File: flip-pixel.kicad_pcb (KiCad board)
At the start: 2 copper layers, 225 parts, among them Q1 DMN62D0U-7, Q10 STS8DN6LF6AG, Q11 DMN62D0U-7, Q12 DMN62D0U-7, Q13 STS8DN6LF6AG, Q14 DMN62D0U-7, Q15 DMN62D0U-7, Q16 STS8DN6LF6AG, Q17 DMN62D0U-7, Q18 DMN62D0U-7, Q19 STS8DN6LF6AG, Q2 DMN62D0U-7, Q20 DMN62D0U-7, Q21 DMN62D0U-7, Q22 STS8DN6LF6AG, Q23 DMN62D0U-7, Q24 DMN62D0U-7, Q25 STS8DN6LF6AG, Q26 DMN62D0U-7, Q27 DMN62D0U-7, Q28 STS8DN6LF6AG, Q29 DMN62D0U-7, Q3 DMN62D0U-7, Q30 DMN62D0U-7, Q31 STS8DN6LF6AG, Q4 STS8DN6LF6AG, Q5 DMN62D0U-7, Q6 DMN62D0U-7, Q7 STS8DN6LF6AG, Q8 DMN62D0U-7, Q9 DMN62D0U-7, U1 LM2665M6

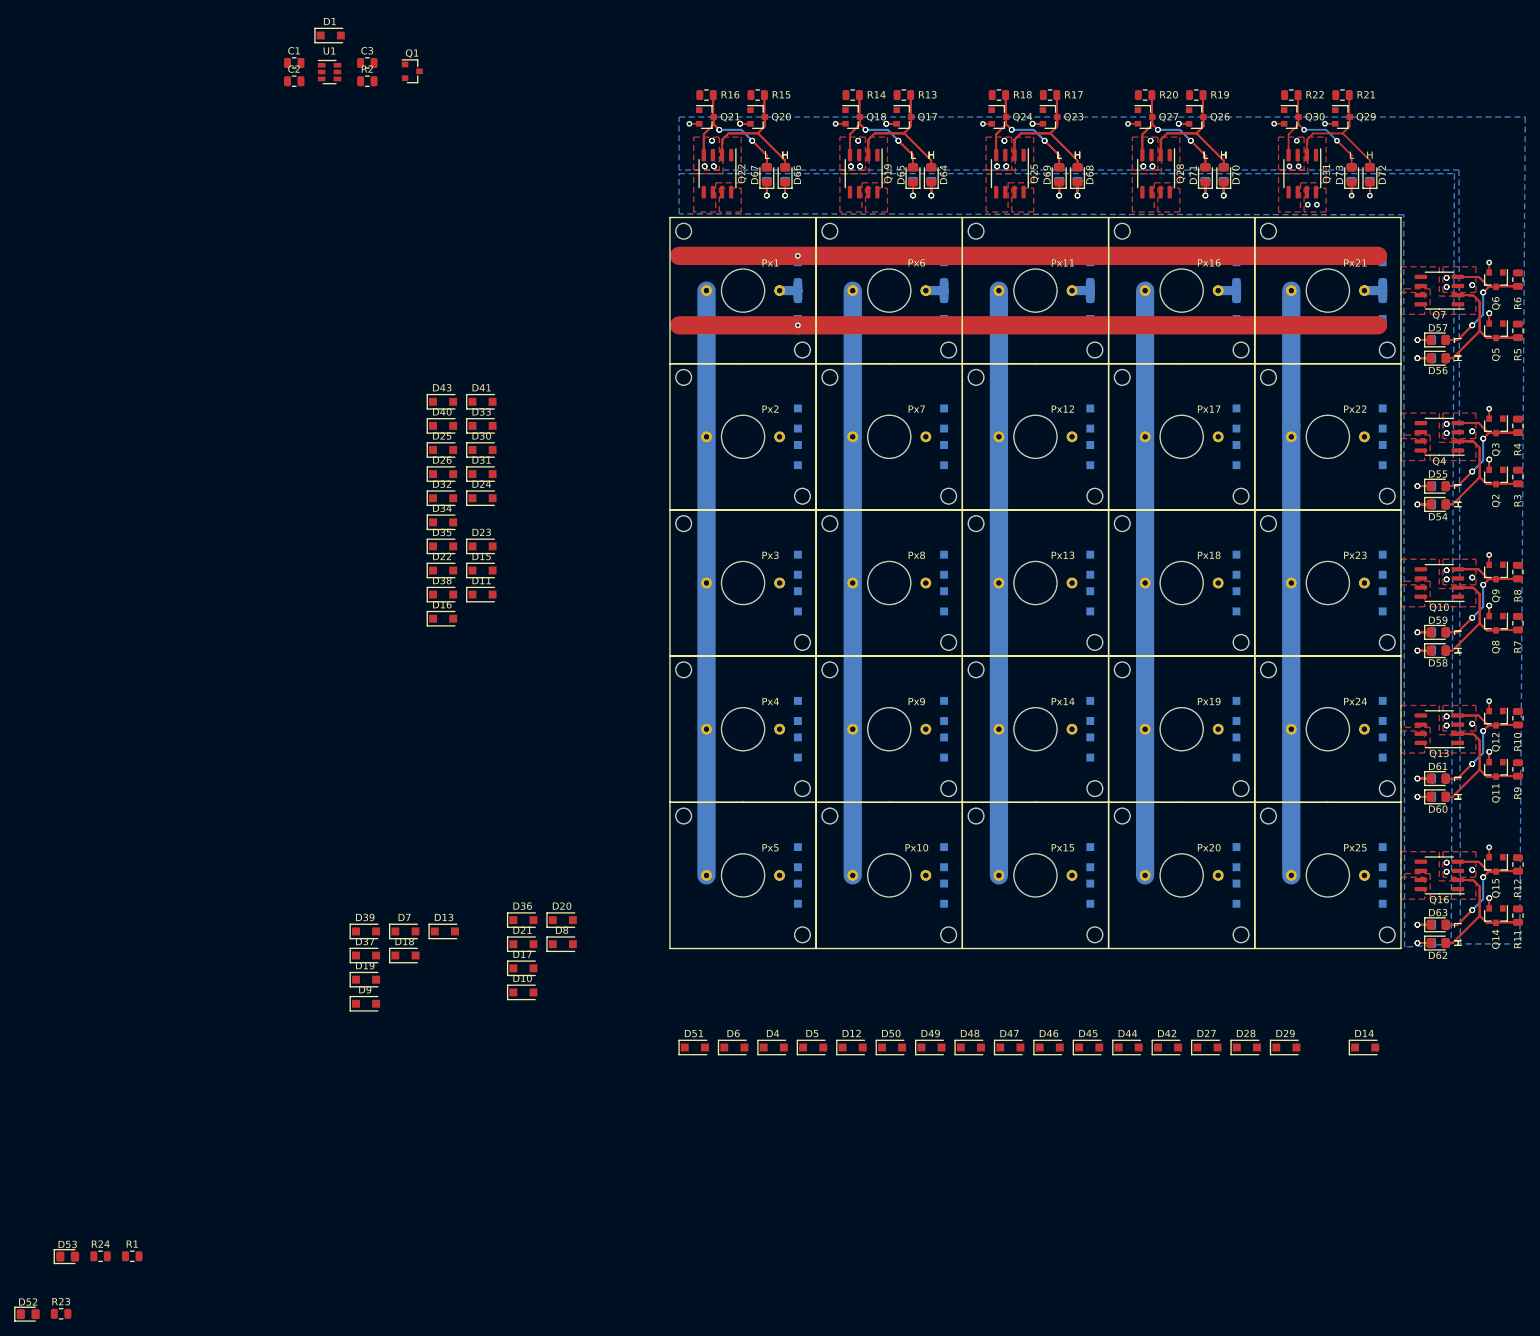
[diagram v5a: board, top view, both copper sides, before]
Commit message: adjustments for row drivers
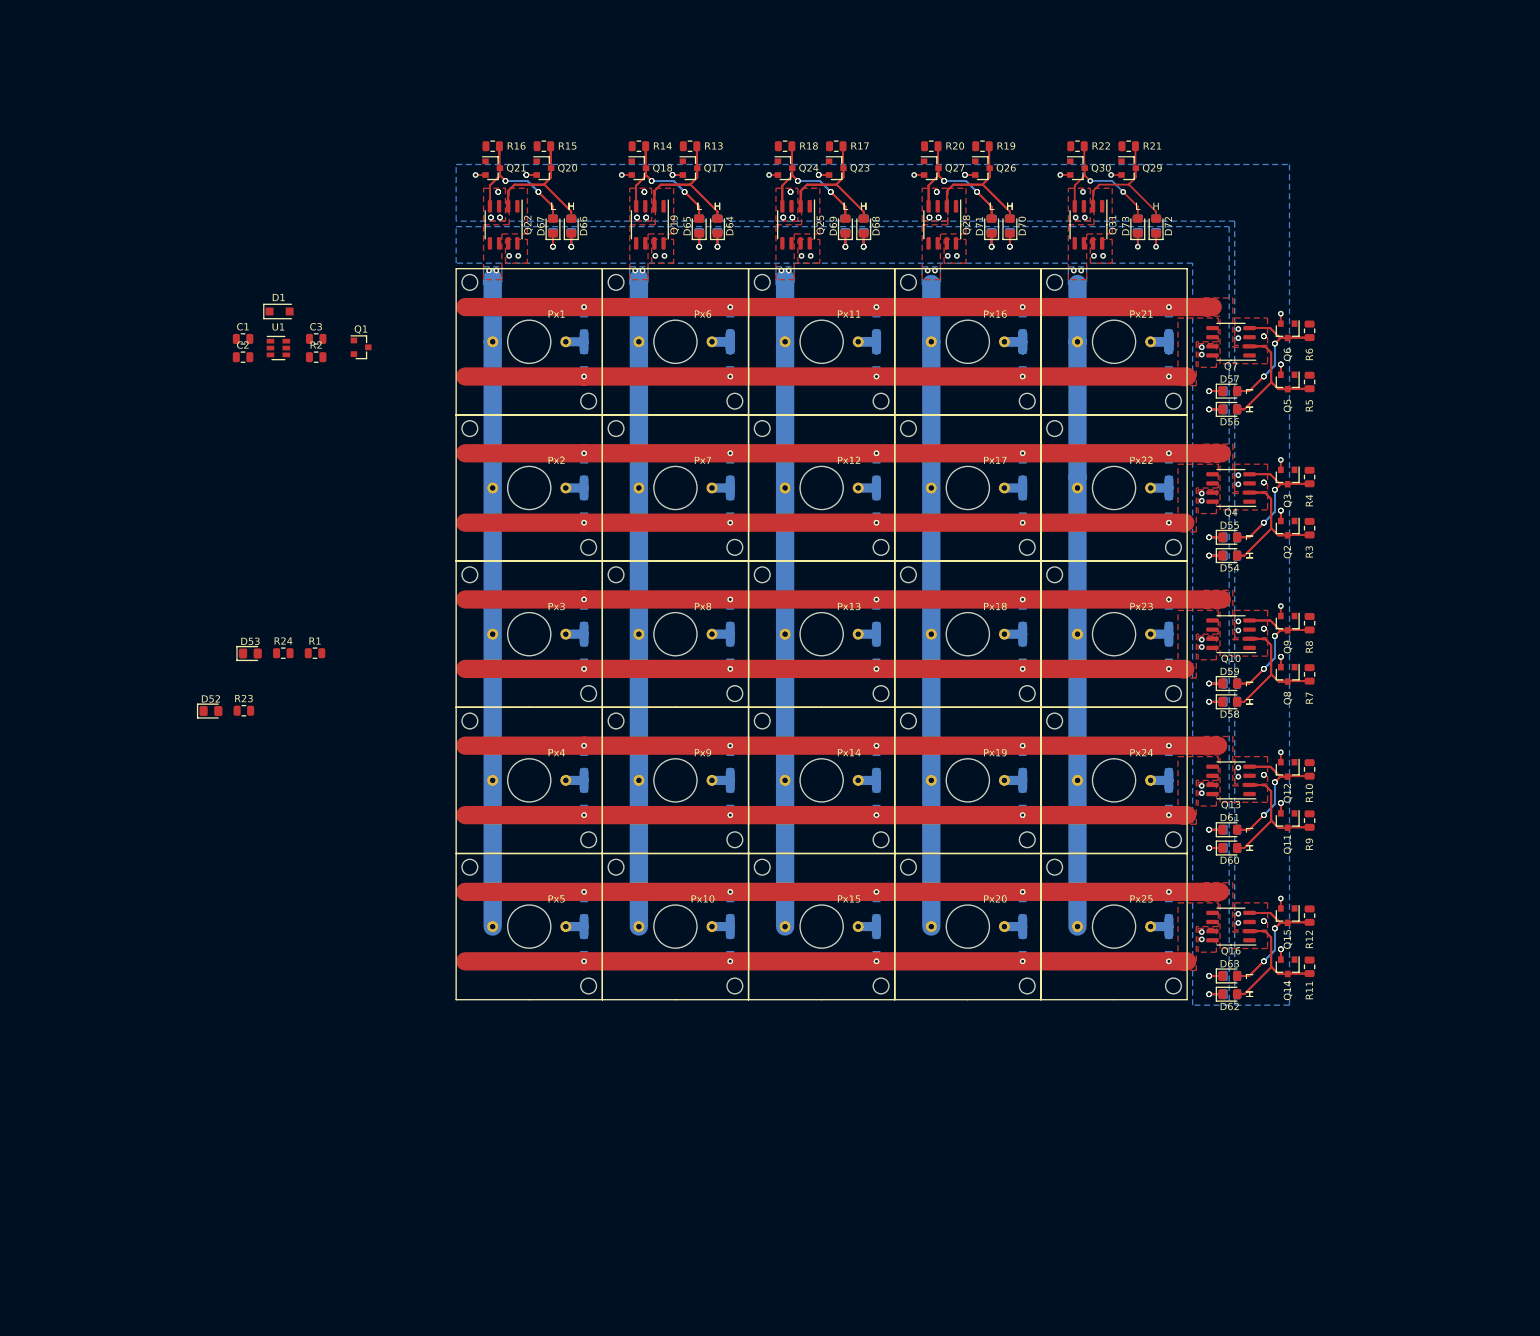
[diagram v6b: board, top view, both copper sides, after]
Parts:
- removed the D10 at (137.1, 149.6)
- removed the D11 at (131.4, 94.3)
- removed the D12 at (182.9, 157.3)
- removed the D13 at (126.2, 141.1)
- removed the D14 at (254.1, 157.3)
- removed the D15 at (131.4, 91.0)
- removed the D16 at (125.9, 97.7)
- removed the D17 at (137.1, 146.3)
- removed the D18 at (120.7, 144.5)
- removed the D19 at (115.2, 147.8)
- removed the D20 at (142.6, 139.6)
- removed the D21 at (137.1, 142.9)
- removed the D22 at (125.9, 91.0)
- removed the D23 at (131.4, 87.6)
- removed the D24 at (131.4, 80.9)
- removed the D25 at (125.9, 74.2)
- removed the D26 at (125.9, 77.6)
- removed the D27 at (232.2, 157.3)
- removed the D28 at (237.7, 157.3)
- removed the D29 at (243.1, 157.3)
- removed the D30 at (131.4, 74.2)
- removed the D31 at (131.4, 77.6)
- removed the D32 at (125.9, 80.9)
- removed the D33 at (131.4, 70.9)
- removed the D34 at (125.9, 84.3)
- removed the D35 at (125.9, 87.6)
- removed the D36 at (137.1, 139.6)
- removed the D37 at (115.2, 144.5)
- removed the D38 at (125.9, 94.3)
- removed the D39 at (115.2, 141.1)
- removed the D4 at (171.9, 157.3)
- removed the D40 at (125.9, 70.9)
- removed the D41 at (131.4, 67.5)
- removed the D42 at (226.7, 157.3)
- removed the D43 at (125.9, 67.5)
- removed the D44 at (221.2, 157.3)
- removed the D45 at (215.7, 157.3)
- removed the D46 at (210.3, 157.3)
- removed the D47 at (204.8, 157.3)
- removed the D48 at (199.3, 157.3)
- removed the D49 at (193.8, 157.3)
- removed the D5 at (177.4, 157.3)
- removed the D50 at (188.3, 157.3)
- removed the D51 at (160.9, 157.3)
- removed the D6 at (166.4, 157.3)
- removed the D7 at (120.7, 141.1)
- removed the D8 at (142.6, 142.9)
- removed the D9 at (115.2, 151.2)
- moved R1 87.6 mm to (108.1, 102.5)
- moved R23 87.6 mm to (98.3, 110.5)
- moved R24 87.6 mm to (103.7, 102.5)
- moved D52 87.6 mm to (93.7, 110.5)
- moved D53 87.6 mm to (99.2, 102.5)
- moved C1 39.0 mm to (98.1, 58.8)
- moved C2 39.0 mm to (98.1, 61.3)
- moved C3 39.0 mm to (108.3, 58.8)
- moved D1 39.0 mm to (103.2, 55.0)
- moved Q1 39.0 mm to (114.6, 59.9)
- moved R2 39.0 mm to (108.3, 61.3)
- moved U1 39.0 mm to (103.1, 60.1)
- moved D12 30.6 mm to (165.9, 56.6)
- moved D13 30.6 mm to (165.9, 61.7)
- moved D14 30.6 mm to (165.9, 77.0)
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- renumbered D2 to D10, D3 to D11, D2 to D12, D3 to D13, D2 to D14, D3 to D15, D2 to D16, D3 to D17, D2 to D18, D3 to D19, D2 to D20, D3 to D21, D2 to D22, D3 to D23, D2 to D24, D3 to D25, D2 to D26, D3 to D27, D2 to D28, D3 to D29, D2 to D30, D3 to D31, D2 to D32, D3 to D33, D2 to D34, D3 to D35, D2 to D36, D3 to D37, D2 to D38, D3 to D39, D2 to D4, D2 to D40, D3 to D41, D2 to D42, D3 to D43, D2 to D44, D3 to D45, D2 to D46, D3 to D47, D2 to D48, D3 to D49, D3 to D5, D2 to D50, D3 to D51, D2 to D6, D3 to D7, D2 to D8, D3 to D9
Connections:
- D10 pad 1: Net-(D2-Pad1) -> Net-(D10-Pad1)
- D10 pad 2: /Row1/High -> /Row5/High
- D11 pad 1: /Row1/Low -> /Row5/Low
- D11 pad 2: Net-(D2-Pad1) -> Net-(D10-Pad1)
- D12 pad 1: Net-(D2-Pad1) -> Net-(D12-Pad1)
- D13 pad 2: Net-(D2-Pad1) -> Net-(D12-Pad1)
- D14 pad 1: Net-(D2-Pad1) -> Net-(D14-Pad1)
- D14 pad 2: /Row1/High -> /Row2/High
- D15 pad 1: /Row1/Low -> /Row2/Low
- D15 pad 2: Net-(D2-Pad1) -> Net-(D14-Pad1)
- D16 pad 1: Net-(D2-Pad1) -> Net-(D16-Pad1)
- D16 pad 2: /Row1/High -> /Row3/High
- D17 pad 1: /Row1/Low -> /Row3/Low
- D17 pad 2: Net-(D2-Pad1) -> Net-(D16-Pad1)
- D18 pad 1: Net-(D2-Pad1) -> Net-(D18-Pad1)
- D18 pad 2: /Row1/High -> /Row4/High
- D19 pad 1: /Row1/Low -> /Row4/Low
- D19 pad 2: Net-(D2-Pad1) -> Net-(D18-Pad1)
- D20 pad 1: Net-(D2-Pad1) -> Net-(D20-Pad1)
- D20 pad 2: /Row1/High -> /Row5/High
- D21 pad 1: /Row1/Low -> /Row5/Low
- D21 pad 2: Net-(D2-Pad1) -> Net-(D20-Pad1)
- D22 pad 1: Net-(D2-Pad1) -> Net-(D22-Pad1)
- D23 pad 2: Net-(D2-Pad1) -> Net-(D22-Pad1)
- D24 pad 1: Net-(D2-Pad1) -> Net-(D24-Pad1)
- D24 pad 2: /Row1/High -> /Row2/High
- D25 pad 1: /Row1/Low -> /Row2/Low
- D25 pad 2: Net-(D2-Pad1) -> Net-(D24-Pad1)
- D26 pad 1: Net-(D2-Pad1) -> Net-(D26-Pad1)
- D26 pad 2: /Row1/High -> /Row3/High
- D27 pad 1: /Row1/Low -> /Row3/Low
- D27 pad 2: Net-(D2-Pad1) -> Net-(D26-Pad1)
- D28 pad 1: Net-(D2-Pad1) -> Net-(D28-Pad1)
- D28 pad 2: /Row1/High -> /Row4/High
- D29 pad 1: /Row1/Low -> /Row4/Low
- D29 pad 2: Net-(D2-Pad1) -> Net-(D28-Pad1)
- D30 pad 1: Net-(D2-Pad1) -> Net-(D30-Pad1)
- D30 pad 2: /Row1/High -> /Row5/High
- D31 pad 1: /Row1/Low -> /Row5/Low
- D31 pad 2: Net-(D2-Pad1) -> Net-(D30-Pad1)
- D32 pad 1: Net-(D2-Pad1) -> Net-(D32-Pad1)
- D33 pad 2: Net-(D2-Pad1) -> Net-(D32-Pad1)
- D34 pad 1: Net-(D2-Pad1) -> Net-(D34-Pad1)
- D34 pad 2: /Row1/High -> /Row2/High
- D35 pad 1: /Row1/Low -> /Row2/Low
- D35 pad 2: Net-(D2-Pad1) -> Net-(D34-Pad1)
- D36 pad 1: Net-(D2-Pad1) -> Net-(D36-Pad1)
- D36 pad 2: /Row1/High -> /Row3/High
- D37 pad 1: /Row1/Low -> /Row3/Low
- D37 pad 2: Net-(D2-Pad1) -> Net-(D36-Pad1)
- D38 pad 1: Net-(D2-Pad1) -> Net-(D38-Pad1)
- D38 pad 2: /Row1/High -> /Row4/High
- D39 pad 1: /Row1/Low -> /Row4/Low
- D39 pad 2: Net-(D2-Pad1) -> Net-(D38-Pad1)
- D4 pad 1: Net-(D2-Pad1) -> Net-(D4-Pad1)
- D4 pad 2: /Row1/High -> /Row2/High
- D40 pad 1: Net-(D2-Pad1) -> Net-(D40-Pad1)
- D40 pad 2: /Row1/High -> /Row5/High
- D41 pad 1: /Row1/Low -> /Row5/Low
- D41 pad 2: Net-(D2-Pad1) -> Net-(D40-Pad1)
- D42 pad 1: Net-(D2-Pad1) -> Net-(D42-Pad1)
- D43 pad 2: Net-(D2-Pad1) -> Net-(D42-Pad1)
- D44 pad 1: Net-(D2-Pad1) -> Net-(D44-Pad1)
- D44 pad 2: /Row1/High -> /Row2/High
- D45 pad 1: /Row1/Low -> /Row2/Low
- D45 pad 2: Net-(D2-Pad1) -> Net-(D44-Pad1)
- D46 pad 1: Net-(D2-Pad1) -> Net-(D46-Pad1)
- D46 pad 2: /Row1/High -> /Row3/High
- D47 pad 1: /Row1/Low -> /Row3/Low
- D47 pad 2: Net-(D2-Pad1) -> Net-(D46-Pad1)
- D48 pad 1: Net-(D2-Pad1) -> Net-(D48-Pad1)
- D48 pad 2: /Row1/High -> /Row4/High
- D49 pad 1: /Row1/Low -> /Row4/Low
- D49 pad 2: Net-(D2-Pad1) -> Net-(D48-Pad1)
- D5 pad 1: /Row1/Low -> /Row2/Low
- D5 pad 2: Net-(D2-Pad1) -> Net-(D4-Pad1)
- D50 pad 1: Net-(D2-Pad1) -> Net-(D50-Pad1)
- D50 pad 2: /Row1/High -> /Row5/High
- D51 pad 1: /Row1/Low -> /Row5/Low
- D51 pad 2: Net-(D2-Pad1) -> Net-(D50-Pad1)
- D6 pad 1: Net-(D2-Pad1) -> Net-(D6-Pad1)
- D6 pad 2: /Row1/High -> /Row3/High
- D7 pad 1: /Row1/Low -> /Row3/Low
- D7 pad 2: Net-(D2-Pad1) -> Net-(D6-Pad1)
- D8 pad 1: Net-(D2-Pad1) -> Net-(D8-Pad1)
- D8 pad 2: /Row1/High -> /Row4/High
- D9 pad 1: /Row1/Low -> /Row4/Low
- D9 pad 2: Net-(D2-Pad1) -> Net-(D8-Pad1)
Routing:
- net /Row3/High: track 0.00 -> 105.2 mm, vias 0 -> 5
- net /Row2/High: track 0.00 -> 105.2 mm, vias 0 -> 5
- net /Row5/High: track 0.00 -> 104.9 mm, vias 0 -> 5
- net /Row4/High: track 0.00 -> 104.6 mm, vias 0 -> 5
- net /Row5/Low: track 0.00 -> 100.3 mm, vias 0 -> 5
- net /Row4/Low: track 0.00 -> 100.3 mm, vias 0 -> 5
- net /Row3/Low: track 0.00 -> 100.1 mm, vias 0 -> 5
- net /Row2/Low: track 0.00 -> 100.1 mm, vias 0 -> 5
- net Net-(D2-Pad1): track 24.1 -> 4.82 mm
- net Net-(D32-Pad1): track 0.00 -> 9.64 mm
- net Net-(D42-Pad1): track 0.00 -> 9.64 mm
- net Net-(D22-Pad1): track 0.00 -> 9.64 mm
- net Net-(D12-Pad1): track 0.00 -> 9.64 mm
- net /PixelMatrix/Col_3: track 81.3 -> 90.2 mm, vias 0 -> 2
- net /PixelMatrix/Col_2: track 81.3 -> 90.2 mm, vias 0 -> 2
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- added copper zone on B.Cu, net /PixelMatrix/Col_3
- added copper zone on B.Cu, net /PixelMatrix/Col_4
- added copper zone on B.Cu, net /PixelMatrix/Col_5
- added copper zone on F.Cu, net /Row1/Low
- added copper zone on F.Cu, net /Row2/Low
- added copper zone on F.Cu, net /Row3/Low
- added copper zone on F.Cu, net /Row4/Low
- added copper zone on F.Cu, net /Row5/Low

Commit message: edge cuts
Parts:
- moved D52 18.0 mm to (106.4, 97.8)
- moved D53 18.0 mm to (111.9, 89.8)
- moved R1 18.0 mm to (120.8, 89.8)
- moved R23 18.0 mm to (111.0, 97.8)
- moved R24 18.0 mm to (116.4, 89.8)
- moved C1 17.0 mm to (105.8, 43.5)
- moved Q1 17.0 mm to (122.2, 44.7)
- moved C2 17.0 mm to (105.8, 46.1)
- moved C3 17.0 mm to (115.9, 43.5)
- moved D1 17.0 mm to (110.8, 39.7)
- moved U1 17.0 mm to (110.7, 44.8)
- moved R2 17.0 mm to (115.9, 46.1)
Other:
- board outline added: 152.4 x 127 mm
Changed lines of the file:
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@@
   (general
     (thickness 1.6)
-    (drawings 38)
+    (drawings 42)
     (tracks 943)
     (zones 0)
@@
     (solder_mask_min_width 0.25)
     (aux_axis_origin 0 0)
-    (visible_elements 7FFE77FF)
+    (visible_elements 7FFFF7FF)
     (pcbplotparams
       (layerselection 0x010fc_ffffffff)
@@
   )
   (module Package_TO_SOT_SMD:SOT-23 (layer F.Cu)
-    (at 114.554 59.944)
+    (at 122.174 44.704)
     (descr "SOT-23, Standard")
     (tags SOT-23)
@@
   )
   (module Capacitor_SMD:C_0805_2012Metric (layer F.Cu)
-    (at 98.148 58.784)
+    (at 105.768 43.544)
     (descr "Capacitor SMD 0805 (2012 Metric), square (rectangular) end terminal, IPC_7351 nominal, (Body size source: https://docs.google.com/spreadsheets/d/1BsfQQcO9C6DZCsRaXUlFlo91Tg2WpOkGARC1WS5S8t0/edit?usp=sharing), generated with kicad-footprint-generator")
     (tags capacitor)
@@
   )
   (module Capacitor_SMD:C_0805_2012Metric (layer F.Cu)
-    (at 98.148 61.324)
+    (at 105.768 46.084)
     (descr "Capacitor SMD 0805 (2012 Metric), square (rectangular) end terminal, IPC_7351 nominal, (Body size source: https://docs.google.com/spreadsheets/d/1BsfQQcO9C6DZCsRaXUlFlo91Tg2WpOkGARC1WS5S8t0/edit?usp=sharing), generated with kicad-footprint-generator")
     (tags capacitor)
@@
   )
   (module Capacitor_SMD:C_0805_2012Metric (layer F.Cu)
-    (at 108.308 58.784)
+    (at 115.928 43.544)
     (descr "Capacitor SMD 0805 (2012 Metric), square (rectangular) end terminal, IPC_7351 nominal, (Body size source: https://docs.google.com/spreadsheets/d/1BsfQQcO9C6DZCsRaXUlFlo91Tg2WpOkGARC1WS5S8t0/edit?usp=sharing), generated with kicad-footprint-generator")
     (tags capacitor)
@@
   )
   (module Diode_SMD:D_SOD-123F (layer F.Cu)
-    (at 103.228 54.974)
+    (at 110.848 39.734)
     (descr D_SOD-123F)
     (tags D_SOD-123F)
@@
   )
   (module LED_SMD:LED_0805_2012Metric_Pad1.15x1.40mm_HandSolder (layer F.Cu)
-    (at 93.684801 110.506001)
+    (at 106.384801 97.806001)
     (descr "LED SMD 0805 (2012 Metric), square (rectangular) end terminal, IPC_7351 nominal, (Body size source: https://docs.google.com/spreadsheets/d/1BsfQQcO9C6DZCsRaXUlFlo91Tg2WpOkGARC1WS5S8t0/edit?usp=sharing), generated with kicad-footprint-generator")
     (tags "LED handsolder")
@@
   )
   (module LED_SMD:LED_0805_2012Metric_Pad1.15x1.40mm_HandSolder (layer F.Cu)
-    (at 99.164801 102.506001)
+    (at 111.864801 89.806001)
     (descr "LED SMD 0805 (2012 Metric), square (rectangular) end terminal, IPC_7351 nominal, (Body size source: https://docs.google.com/spreadsheets/d/1BsfQQcO9C6DZCsRaXUlFlo91Tg2WpOkGARC1WS5S8t0/edit?usp=sharing), generated with kicad-footprint-generator")
     (tags "LED handsolder")
@@
   )
   (module Resistor_SMD:R_0805_2012Metric (layer F.Cu)
-    (at 108.149801 102.461001)
+    (at 120.849801 89.761001)
     (descr "Resistor SMD 0805 (2012 Metric), square (rectangular) end terminal, IPC_7351 nominal, (Body size source: https://docs.google.com/spreadsheets/d/1BsfQQcO9C6DZCsRaXUlFlo91Tg2WpOkGARC1WS5S8t0/edit?usp=sharing), generated with kicad-footprint-generator")
     (tags resistor)
@@
   )
   (module Resistor_SMD:R_0805_2012Metric (layer F.Cu)
-    (at 108.308 61.324)
+    (at 115.928 46.084)
     (descr "Resistor SMD 0805 (2012 Metric), square (rectangular) end terminal, IPC_7351 nominal, (Body size source: https://docs.google.com/spreadsheets/d/1BsfQQcO9C6DZCsRaXUlFlo91Tg2WpOkGARC1WS5S8t0/edit?usp=sharing), generated with kicad-footprint-generator")
     (tags resistor)
@@
   )
   (module Resistor_SMD:R_0805_2012Metric (layer F.Cu)
-    (at 98.259801 110.461001)
+    (at 110.959801 97.761001)
     (descr "Resistor SMD 0805 (2012 Metric), square (rectangular) end terminal, IPC_7351 nominal, (Body size source: https://docs.google.com/spreadsheets/d/1BsfQQcO9C6DZCsRaXUlFlo91Tg2WpOkGARC1WS5S8t0/edit?usp=sharing), generated with kicad-footprint-generator")
     (tags resistor)
@@
   )
   (module Resistor_SMD:R_0805_2012Metric (layer F.Cu)
-    (at 103.739801 102.461001)
+    (at 116.439801 89.761001)
     (descr "Resistor SMD 0805 (2012 Metric), square (rectangular) end terminal, IPC_7351 nominal, (Body size source: https://docs.google.com/spreadsheets/d/1BsfQQcO9C6DZCsRaXUlFlo91Tg2WpOkGARC1WS5S8t0/edit?usp=sharing), generated with kicad-footprint-generator")
     (tags resistor)
@@
   )
   (module Package_TO_SOT_SMD:SOT-23-6 (layer F.Cu)
-    (at 103.058 60.054)
+    (at 110.678 44.814)
     (descr "6-pin SOT-23 package")
     (tags SOT-23-6)
@@
     )
   )
+  (gr_line (start 248.92 27.94) (end 248.92 154.94) (layer Edge.Cuts) (width 0.05))
+  (gr_line (start 96.52 27.94) (end 248.92 27.94) (layer Edge.Cuts) (width 0.05))
+  (gr_line (start 96.52 154.94) (end 96.52 27.94) (layer Edge.Cuts) (width 0.05))
+  (gr_line (start 248.92 154.94) (end 96.52 154.94) (layer Edge.Cuts) (width 0.05))
   (gr_text L (at 237.998 147.32 -90) (layer F.SilkS)
     (effects (font (size 1 1) (thickness 0.15)))

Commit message: Added 3D model to Power FET footprint
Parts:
- Q10, Q13, Q16, Q19, Q22, Q25, Q28, Q31, Q4, Q7: footprint Package_SO:SO-8_3.9x4.9mm_P1.27mm -> Custom-Footprints:SO-8_3.9x4.9mm_P1.27mm
